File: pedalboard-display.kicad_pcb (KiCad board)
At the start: 2 copper layers, 174 x 111 mm, 203 parts, among them J1 Conn_01x03_Pin, J2 Conn_01x03_Pin

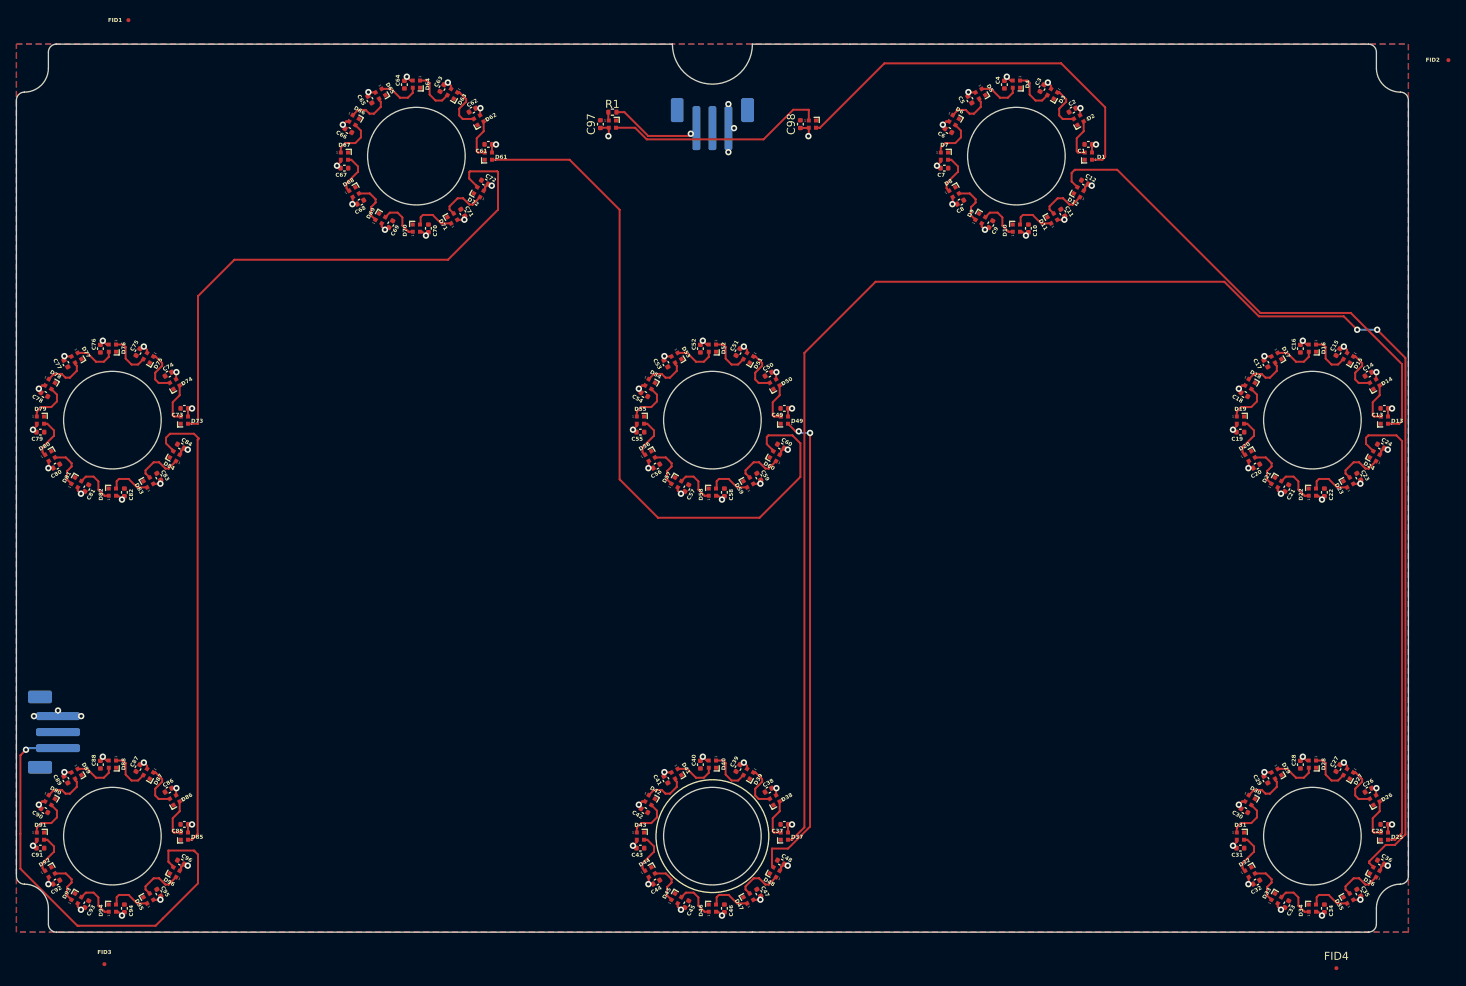
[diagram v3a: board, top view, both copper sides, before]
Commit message: Place fiducials
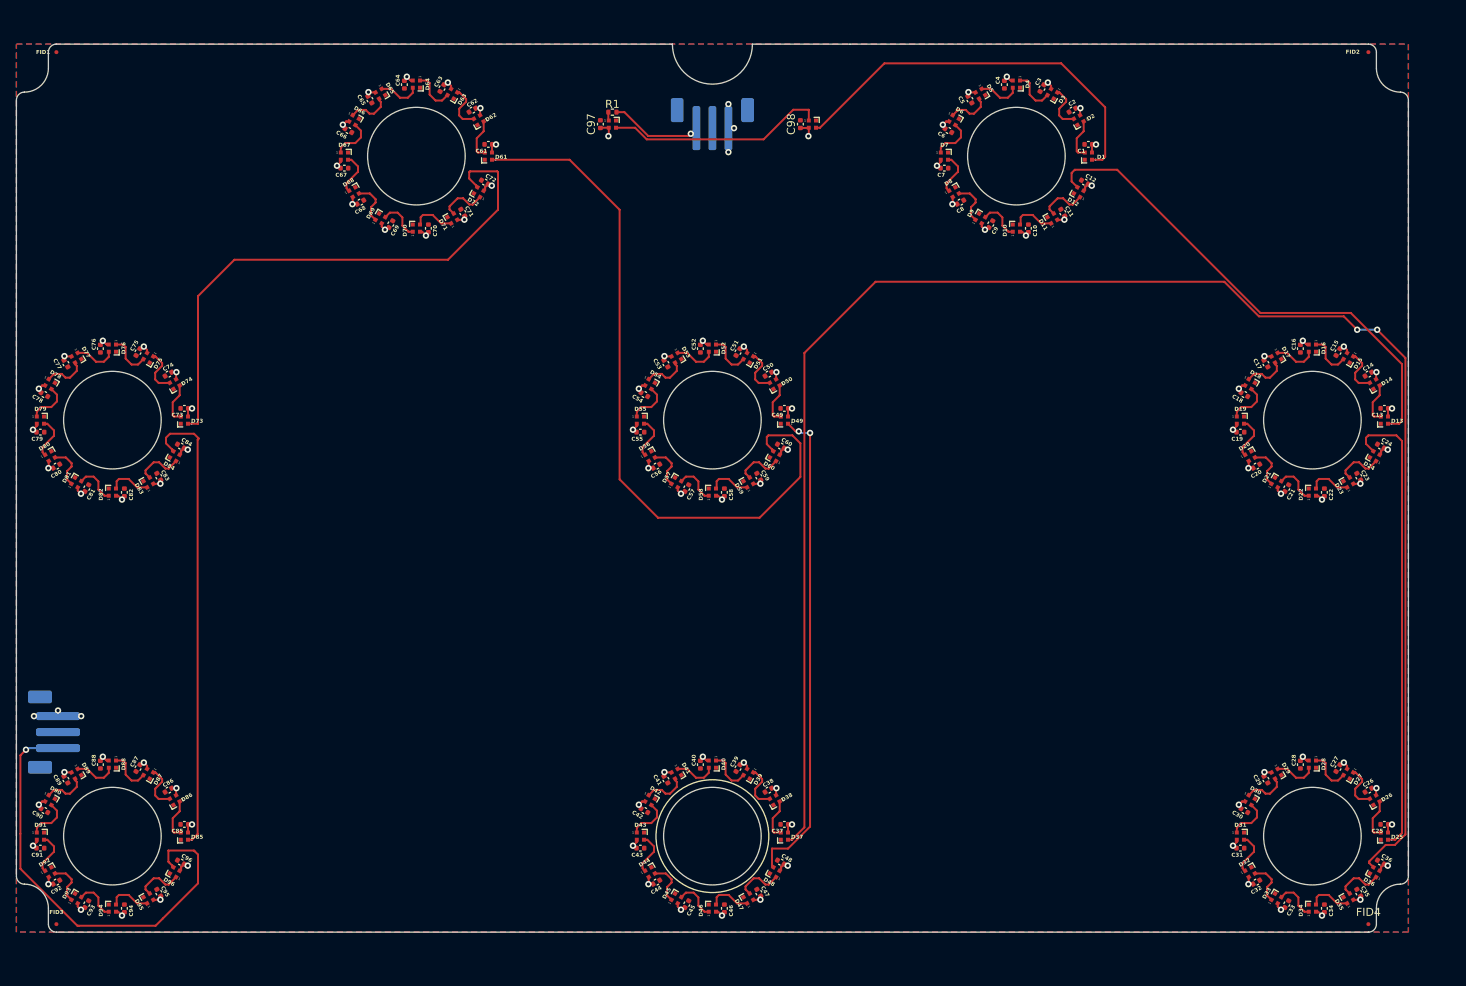
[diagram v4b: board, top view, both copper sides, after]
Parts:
- moved FID2 10.0 mm to (189.0, 26.0)
- moved FID1 9.85 mm to (25.0, 26.0)
- moved FID3 7.81 mm to (25.0, 135.0)
- moved FID4 6.80 mm to (189.0, 135.0)
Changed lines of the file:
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@@
   (net 102 "Net-(D97-DOUT)")
   (footprint "Fiducial:Fiducial_0.5mm_Mask1mm" (layer "F.Cu")
-    (at 199 27)
+    (at 189 26)
     (descr "Circular Fiducial, 0.5mm bare copper, 1mm soldermask opening (Level C)")
     (tags "fiducial")
@@
   )
   (footprint "Fiducial:Fiducial_0.5mm_Mask1mm" (layer "F.Cu")
-    (at 34 22)
+    (at 25 26)
     (descr "Circular Fiducial, 0.5mm bare copper, 1mm soldermask opening (Level C)")
     (tags "fiducial")
@@
   )
   (footprint "Fiducial:Fiducial_0.5mm_Mask1mm" (layer "F.Cu")
-    (at 185 140.5)
+    (at 189 135)
     (descr "Circular Fiducial, 0.5mm bare copper, 1mm soldermask opening (Level C)")
     (tags "fiducial")
@@
   )
   (footprint "Fiducial:Fiducial_0.5mm_Mask1mm" (layer "F.Cu")
-    (at 31 140)
+    (at 25 135)
     (descr "Circular Fiducial, 0.5mm bare copper, 1mm soldermask opening (Level C)")
     (tags "fiducial")
